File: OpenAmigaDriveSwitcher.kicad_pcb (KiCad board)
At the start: 2 copper layers, 25.1 x 52.3 mm, 7 parts, among them J1 PADS, J2 SWITCH, J99 OSHW_LOGO, U1 74LS157, U8 EVEN_CIA_CHIP

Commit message: Reduce clearance
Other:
- net class Default: clearance 0.2 -> 0.15
- net class Power: clearance 0.25 -> 0.15
- rule trace_clearance: 0.2 -> 0.15
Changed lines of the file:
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@@
   (setup
     (last_trace_width 0.25)
-    (trace_clearance 0.2)
+    (trace_clearance 0.15)
     (zone_clearance 0.1)
     (zone_45_only no)
@@
   (net 43 "Net-(U1-Pad3)")
   (net_class Default "This is the default net class."
-    (clearance 0.2)
+    (clearance 0.15)
     (trace_width 0.25)
     (via_dia 0.6)
@@
   )
   (net_class Power ""
-    (clearance 0.25)
+    (clearance 0.15)
     (trace_width 0.5)
     (via_dia 0.8)

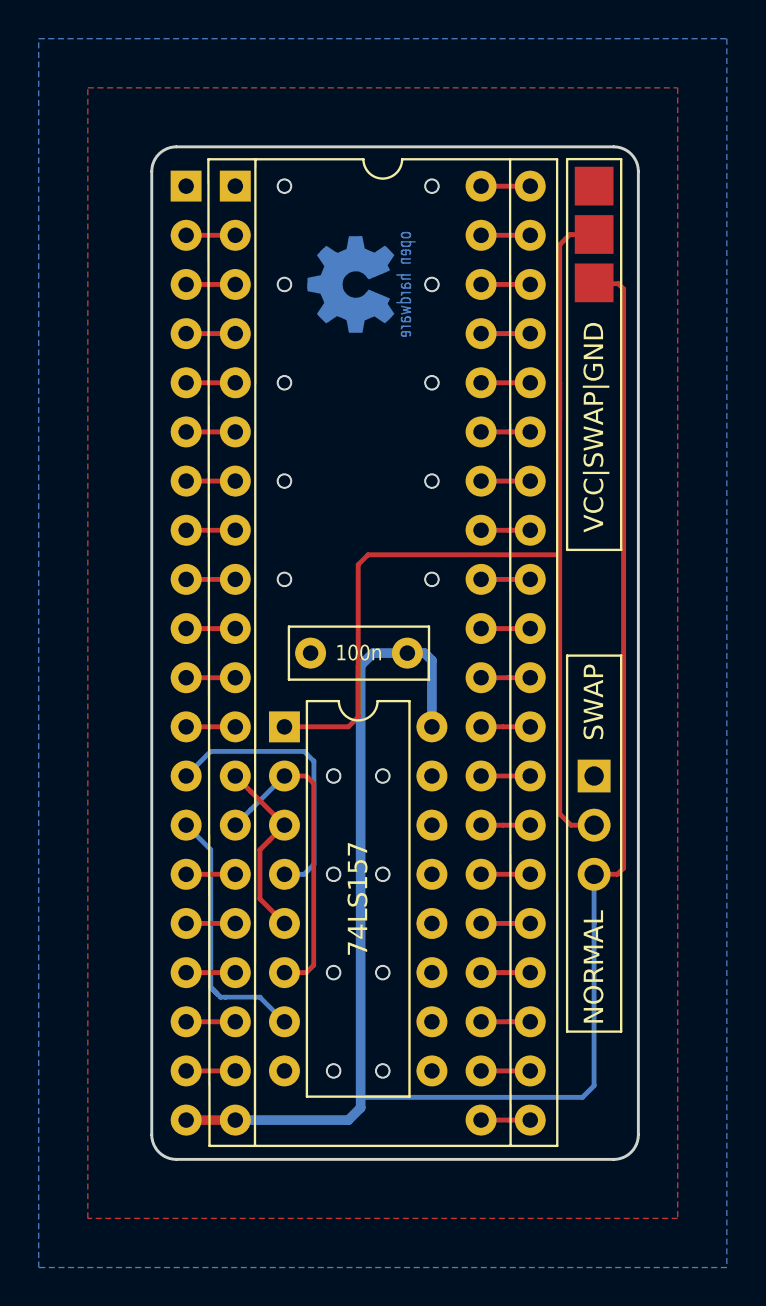
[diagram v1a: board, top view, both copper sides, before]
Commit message: Allow swapping DF0 <-> DF2
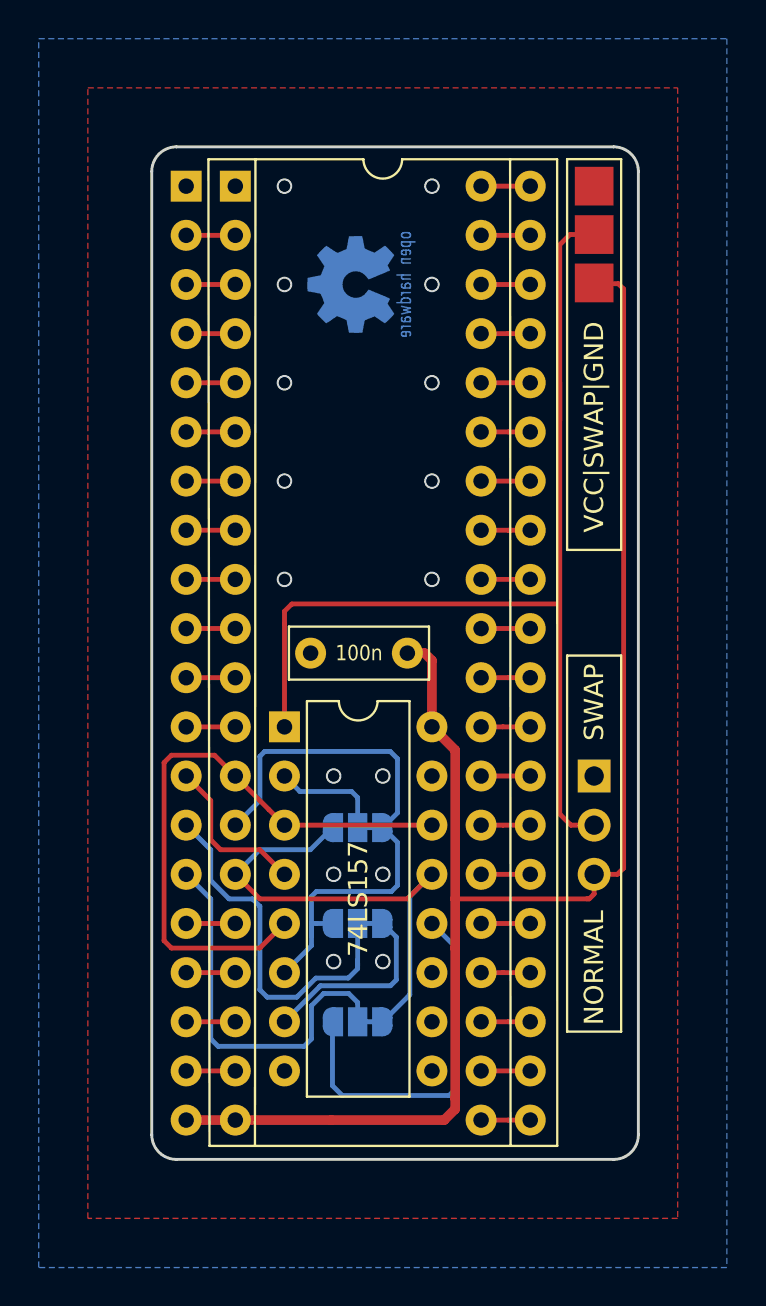
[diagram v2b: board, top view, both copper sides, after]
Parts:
- added J0: SW_INPUT, OpenAmigaDriveSwitcher:SolderJumper-3_P1.3mm_Bridged12_RoundedPad1.0x1.5mm, B.Cu at (151.1, 137.3)
- added J1: SW_SEL1, OpenAmigaDriveSwitcher:SolderJumper-3_P1.3mm_Bridged12_RoundedPad1.0x1.5mm, B.Cu at (151.1, 142.2)
- added J2: SW_SEL2, OpenAmigaDriveSwitcher:SolderJumper-3_P1.3mm_Bridged12_RoundedPad1.0x1.5mm, B.Cu at (151.1, 147.3)
- J10: renamed from J2; value SWITCH -> CMD_SWITCH
- J11: renamed from J1; value PADS -> CMD_PADS
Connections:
- net Net-(CONN1-Pad13) renamed /~sel0_out
- net Net-(CONN1-Pad16) renamed /~sel3
- net Net-(CONN1-Pad17) renamed /~mtr
- net Net-(CONN1-Pad18) renamed /pin18
- net Net-(CONN1-Pad19) renamed /pin19
- net Net-(CONN1-Pad21) renamed /pin21
- net Net-(CONN1-Pad22) renamed /pin22
- net Net-(CONN1-Pad23) renamed /pin23
- net Net-(CONN1-Pad24) renamed /pin24
- net Net-(CONN1-Pad25) renamed /pin25
- net Net-(CONN1-Pad26) renamed /pin26
- net Net-(CONN1-Pad27) renamed /pin27
- net Net-(CONN1-Pad28) renamed /pin28
- net Net-(CONN1-Pad29) renamed /pin29
- net Net-(CONN1-Pad30) renamed /pin30
- net Net-(CONN1-Pad31) renamed /pin31
- net Net-(CONN1-Pad32) renamed /pin32
- net Net-(CONN1-Pad33) renamed /pin33
- net Net-(CONN1-Pad34) renamed /pin34
- net Net-(CONN1-Pad35) renamed /pin35
- net Net-(CONN1-Pad36) renamed /pin36
- net Net-(CONN1-Pad37) renamed /pin37
- net Net-(CONN1-Pad38) renamed /pin38
- net Net-(CONN1-Pad39) renamed /pin39
- net Net-(CONN1-Pad40) renamed /pin40
- CONN1 pad 14: Net-(CONN1-Pad14) -> /~sel1_out
- CONN1 pad 15: Net-(CONN1-Pad15) -> /~sel2_out
- U1 pad 12: (no net) -> Net-(J2-Pad3)
- U1 pad 13: GND -> /~sel2
- U1 pad 14: GND -> /~sel0
- U1 pad 2: Net-(U1-Pad2) -> /~sel1_2
- U1 pad 3: Net-(U1-Pad3) -> /~sel0
- U1 pad 5: Net-(U1-Pad3) -> /~sel0
- U1 pad 6: Net-(U1-Pad2) -> /~sel1
- U1 pad 7: Net-(CONN1-Pad14) -> Net-(J1-Pad1)
- U8 pad 13: Net-(U1-Pad3) -> /~sel0
- U8 pad 14: Net-(U1-Pad2) -> /~sel1
- U8 pad 15: Net-(CONN1-Pad15) -> /~sel2
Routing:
- net /~sel0: track 0.00 -> 31.6 mm
- net /~sel1: track 0.00 -> 29.3 mm
- net /~sel2: track 0.00 -> 25.9 mm
- net /~sel2_out: track 0.00 -> 20.1 mm
- net Net-(J2-Pad3): track 0.00 -> 19.1 mm
- net /~sel1_out: track 0.00 -> 19.1 mm
- net Net-(U1-Pad2): track 16.3 -> 0.00 mm
- net VCC: track 96.1 -> 80.8 mm
- net Net-(CONN1-Pad14): track 14.0 -> 0.00 mm
- net Net-(J1-Pad1): track 0.00 -> 9.88 mm
- net Net-(U1-Pad3): track 9.72 -> 0.00 mm
- net /~sel0_out: track 14.4 -> 8.37 mm
- net /~sel1_2: track 0.00 -> 5.80 mm
- net Net-(CONN1-Pad15): track 2.54 -> 0.00 mm
- net Net-(J10-Pad2): track 57.9 -> 55.7 mm
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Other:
- board text added: "DF1"
- board text added: "DF2"
- board text added: "V3"
- board text added: "github.com/SukkoPera/ OpenAmigaDriveSwitcher"
- board text removed: "V2"
- board text removed: "github.com/SukkoPera/OpenAmigaDriveSwitcher"

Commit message: Add OHL claim
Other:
- board text added: "Licensed under CERN OHL v.1.2"
- board text added: "github.com/SukkoPera/OpenAmigaDriveSwitcher"
- board text removed: "github.com/SukkoPera/ OpenAmigaDriveSwitcher"
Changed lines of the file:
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@@
-(kicad_pcb (version 20171130) (host pcbnew 5.0.0)
+(kicad_pcb (version 20171130) (host pcbnew 5.0.2)
   (general
     (thickness 1.6)
-    (drawings 34)
+    (drawings 35)
     (tracks 185)
     (zones 0)
@@
     (pad_drill 0.8)
     (pad_to_mask_clearance 0)
+    (solder_mask_min_width 0.25)
     (aux_axis_origin 140.462 154.432)
     (visible_elements FFFFFF7F)
@@
       ))
   )
+  (gr_text "Licensed under CERN OHL v.1.2" (at 162.306 112.522 90) (layer B.SilkS)
+    (effects (font (size 0.8 0.8) (thickness 0.15)) (justify mirror))
+  )
   (gr_arc (start 148.844 134.112) (end 148.844 133.731) (angle -90) (layer B.SilkS) (width 0.12))
   (gr_arc (start 153.416 134.112) (end 153.797 134.112) (angle -90) (layer B.SilkS) (width 0.12))
@@
   )
   (gr_text V3 (at 164.338 152.781 90) (layer B.SilkS)
-    (effects (font (size 1 1) (thickness 0.15)) (justify mirror))
-  )
-  (gr_text "github.com/SukkoPera/\nOpenAmigaDriveSwitcher" (at 163.068 112.649 90) (layer B.SilkS)
-    (effects (font (size 1 1) (thickness 0.15)) (justify mirror))
+    (effects (font (size 0.8 0.8) (thickness 0.15)) (justify mirror))
+  )
+  (gr_text github.com/SukkoPera/OpenAmigaDriveSwitcher (at 163.83 117.348 90) (layer B.SilkS)
+    (effects (font (size 0.8 0.8) (thickness 0.15)) (justify mirror))
   )
   (gr_line (start 164.719 128.397) (end 164.719 147.828) (layer F.SilkS) (width 0.12))
@@
   (via (at 152.4 144.2085) (size 0.8) (drill 0.6) (layers F.Cu B.Cu) (net 2))
   (via (at 149.86 144.2085) (size 0.8) (drill 0.6) (layers F.Cu B.Cu) (net 2))
+  (segment (start 142.24 106.68) (end 144.78 106.68) (width 0.25) (layer F.Cu) (net 3) (status 30))
+  (segment (start 142.24 109.22) (end 144.78 109.22) (width 0.25) (layer F.Cu) (net 4) (status 30))
+  (segment (start 142.24 111.76) (end 144.78 111.76) (width 0.25) (layer F.Cu) (net 5) (status 30))
+  (segment (start 142.24 114.3) (end 143.37137 114.3) (width 0.25) (layer F.Cu) (net 6) (status 10))
+  (segment (start 143.37137 114.3) (end 144.78 114.3) (width 0.25) (layer F.Cu) (net 6) (status 20))
+  (segment (start 142.24 116.84) (end 143.37137 116.84) (width 0.25) (layer F.Cu) (net 7) (status 10))
+  (segment (start 143.37137 116.84) (end 144.78 116.84) (width 0.25) (layer F.Cu) (net 7) (status 20))
+  (segment (start 142.24 119.38) (end 144.78 119.38) (width 0.25) (layer F.Cu) (net 8) (status 30))
+  (segment (start 142.24 121.92) (end 144.78 121.92) (width 0.25) (layer F.Cu) (net 9) (status 30))
+  (segment (start 142.24 124.46) (end 144.78 124.46) (width 0.25) (layer F.Cu) (net 10) (status 30))
+  (segment (start 142.24 127) (end 143.37137 127) (width 0.25) (layer F.Cu) (net 11) (status 10))
+  (segment (start 143.37137 127) (end 144.78 127) (width 0.25) (layer F.Cu) (net 11) (status 20))
+  (segment (start 142.24 129.54) (end 144.78 129.54) (width 0.25) (layer F.Cu) (net 12) (status 30))
+  (segment (start 142.24 132.08) (end 144.78 132.08) (width 0.25) (layer F.Cu) (net 13) (status 30))
   (segment (start 157.48 149.86) (end 160.02 149.86) (width 0.25) (layer F.Cu) (net 14) (status 30))
-  (segment (start 142.24 106.68) (end 144.78 106.68) (width 0.25) (layer F.Cu) (net 3) (status 30))
   (segment (start 160.02 147.32) (end 158.88863 147.32) (width 0.25) (layer F.Cu) (net 15) (status 10))
   (segment (start 158.88863 147.32) (end 157.48 147.32) (width 0.25) (layer F.Cu) (net 15) (status 20))
-  (segment (start 142.24 109.22) (end 144.78 109.22) (width 0.25) (layer F.Cu) (net 4) (status 30))
   (segment (start 157.48 144.78) (end 158.61137 144.78) (width 0.25) (layer F.Cu) (net 16) (status 10))
   (segment (start 158.61137 144.78) (end 160.02 144.78) (width 0.25) (layer F.Cu) (net 16) (status 20))
-  (segment (start 142.24 111.76) (end 144.78 111.76) (width 0.25) (layer F.Cu) (net 5) (status 30))
   (segment (start 160.02 142.24) (end 157.48 142.24) (width 0.25) (layer F.Cu) (net 17) (status 30))
-  (segment (start 142.24 114.3) (end 143.37137 114.3) (width 0.25) (layer F.Cu) (net 6) (status 10))
-  (segment (start 143.37137 114.3) (end 144.78 114.3) (width 0.25) (layer F.Cu) (net 6) (status 20))
   (segment (start 157.48 139.7) (end 160.02 139.7) (width 0.25) (layer F.Cu) (net 18) (status 30))
-  (segment (start 142.24 116.84) (end 143.37137 116.84) (width 0.25) (layer F.Cu) (net 7) (status 10))
-  (segment (start 143.37137 116.84) (end 144.78 116.84) (width 0.25) (layer F.Cu) (net 7) (status 20))
   (segment (start 157.48 137.16) (end 158.61137 137.16) (width 0.25) (layer F.Cu) (net 19) (status 10))
   (segment (start 158.61137 137.16) (end 160.02 137.16) (width 0.25) (layer F.Cu) (net 19) (status 20))
-  (segment (start 142.24 119.38) (end 144.78 119.38) (width 0.25) (layer F.Cu) (net 8) (status 30))
   (segment (start 157.48 134.62) (end 160.02 134.62) (width 0.25) (layer F.Cu) (net 20) (status 30))
-  (segment (start 142.24 121.92) (end 144.78 121.92) (width 0.25) (layer F.Cu) (net 9) (status 30))
   (segment (start 157.48 132.08) (end 158.61137 132.08) (width 0.25) (layer F.Cu) (net 21) (status 10))
   (segment (start 158.61137 132.08) (end 160.02 132.08) (width 0.25) (layer F.Cu) (net 21) (status 20))
-  (segment (start 142.24 124.46) (end 144.78 124.46) (width 0.25) (layer F.Cu) (net 10) (status 30))
   (segment (start 160.02 129.54) (end 158.88863 129.54) (width 0.25) (layer F.Cu) (net 22) (status 10))
   (segment (start 158.88863 129.54) (end 157.48 129.54) (width 0.25) (layer F.Cu) (net 22) (status 20))
-  (segment (start 142.24 127) (end 143.37137 127) (width 0.25) (layer F.Cu) (net 11) (status 10))
-  (segment (start 143.37137 127) (end 144.78 127) (width 0.25) (layer F.Cu) (net 11) (status 20))
   (segment (start 157.48 127) (end 160.02 127) (width 0.25) (layer F.Cu) (net 23) (status 30))
-  (segment (start 142.24 129.54) (end 144.78 129.54) (width 0.25) (layer F.Cu) (net 12) (status 30))
   (segment (start 157.48 124.46) (end 160.02 124.46) (width 0.25) (layer F.Cu) (net 24) (status 30))
-  (segment (start 142.24 132.08) (end 144.78 132.08) (width 0.25) (layer F.Cu) (net 13) (status 30))
   (segment (start 160.02 121.92) (end 158.88863 121.92) (width 0.25) (layer F.Cu) (net 25) (status 10))
   (segment (start 158.88863 121.92) (end 157.48 121.92) (width 0.25) (layer F.Cu) (net 25) (status 20))

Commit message: Ready for V3
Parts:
- removed J99: OSHW_LOGO, w_logo:Logo_copper_OSHW_6x6mm
- added P99: OSHW_LOGO, Symbol:OSHW-Logo_5.7x6mm_Copper, B.Cu at (151.1, 109.2)
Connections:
- U1 pad 9: (no net) -> Net-(U1-Pad9)
